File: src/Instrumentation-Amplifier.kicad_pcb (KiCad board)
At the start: 2 copper layers, 24.1 x 34.3 mm, 10 parts, among them J1 PPTC041LFBN-RC, J2 PPTC041LFBN-RC, U1 LM7812_SMD, U2 AD623ARZ-R7

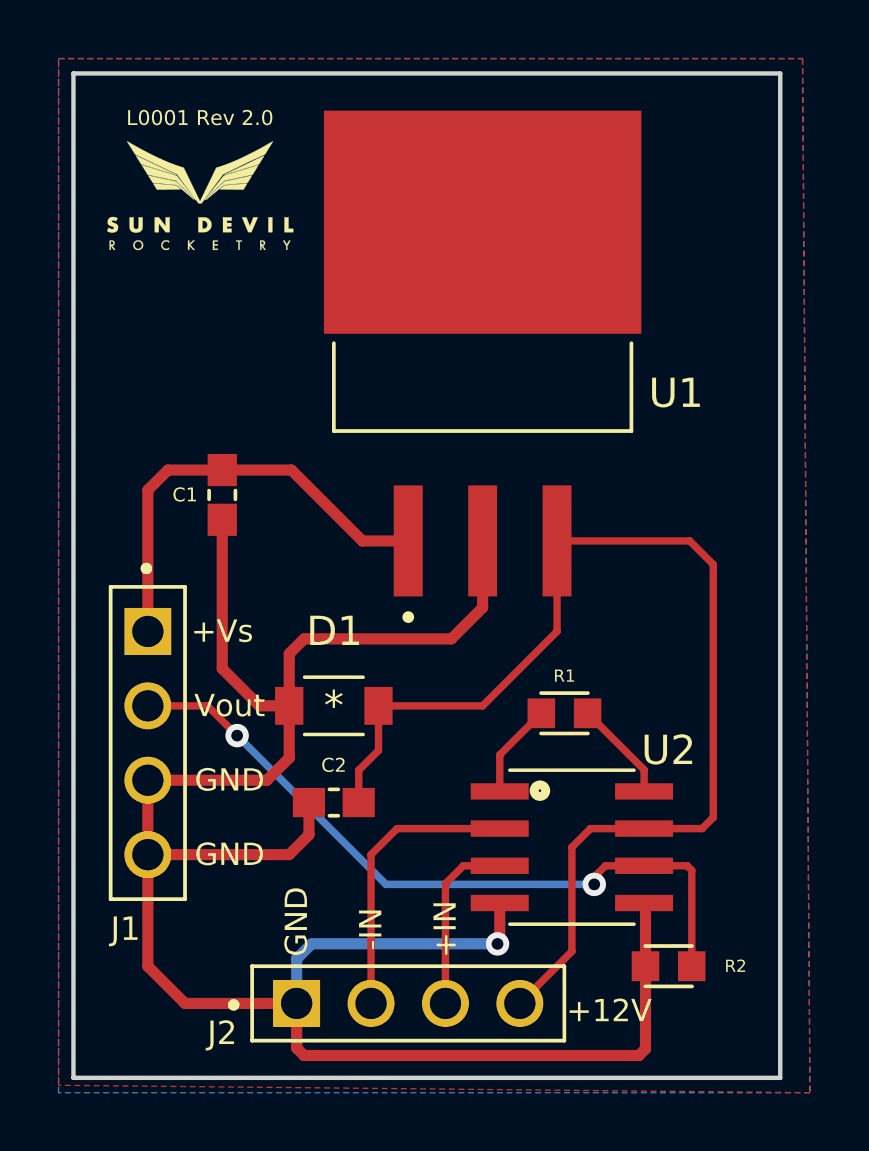
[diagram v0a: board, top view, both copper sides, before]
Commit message: Fixed issue with decoupling cap placement
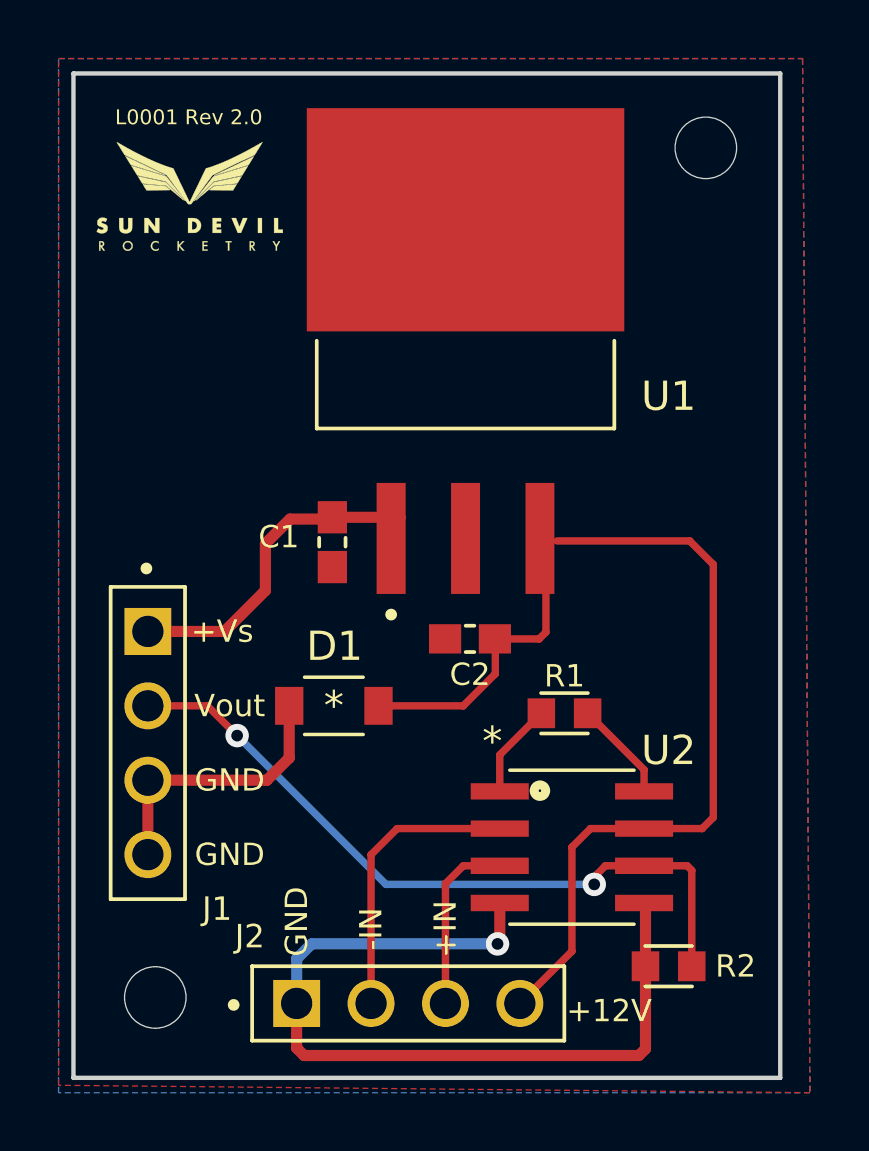
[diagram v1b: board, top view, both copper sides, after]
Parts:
- added REF**: MountingHole_2.1mm, Instrumentation-Amplifier:MountingHole_2.1mm, F.Cu at (106.9, 131.9)
- added REF**: MountingHole_2.1mm, Instrumentation-Amplifier:MountingHole_2.1mm, F.Cu at (125.7, 102.9)
- D1: value LTST-C150GKT -> LED_LTST-C150GKT_LTO
- U2: value AD623ARZ-R7 -> R_8_ADI
- moved C2 7.27 mm to (117.7, 119.6)
- moved C1 4.09 mm to (113.0, 116.3)
- moved U1 0.59 mm to (117.5, 109.8)
- moved G*** 0.36 mm to (108.1, 104.4)
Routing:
- net Earth: track 73.6 -> 38.1 mm
- net ~: track 39.4 -> 35.2 mm
- net /+Vs: track 15.0 -> 11.2 mm
